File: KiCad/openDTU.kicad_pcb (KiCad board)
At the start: 2 copper layers, 50 x 50 mm, 12 parts, among them U1 ESP32NodeMCU, U2 NRF24L01+PA+LNA_Breakout

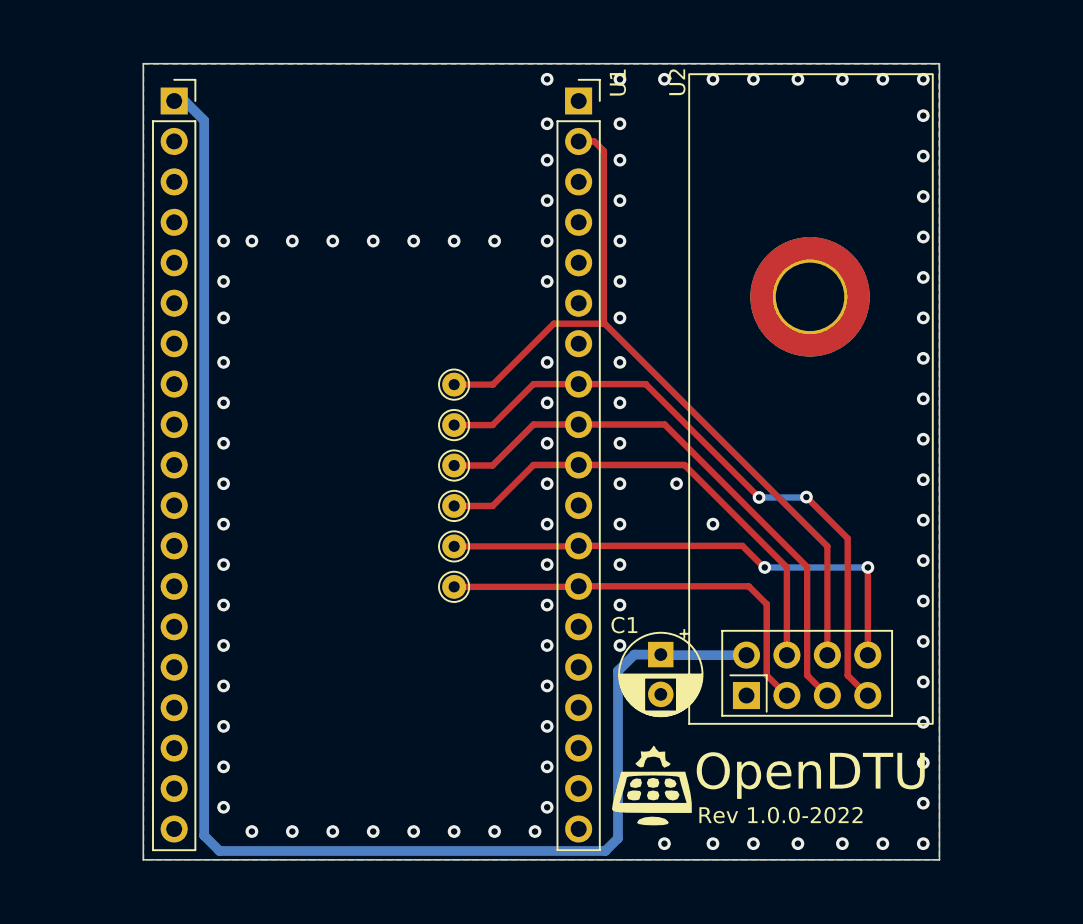
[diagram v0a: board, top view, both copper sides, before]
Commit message: Added mounting holes and some other improvments
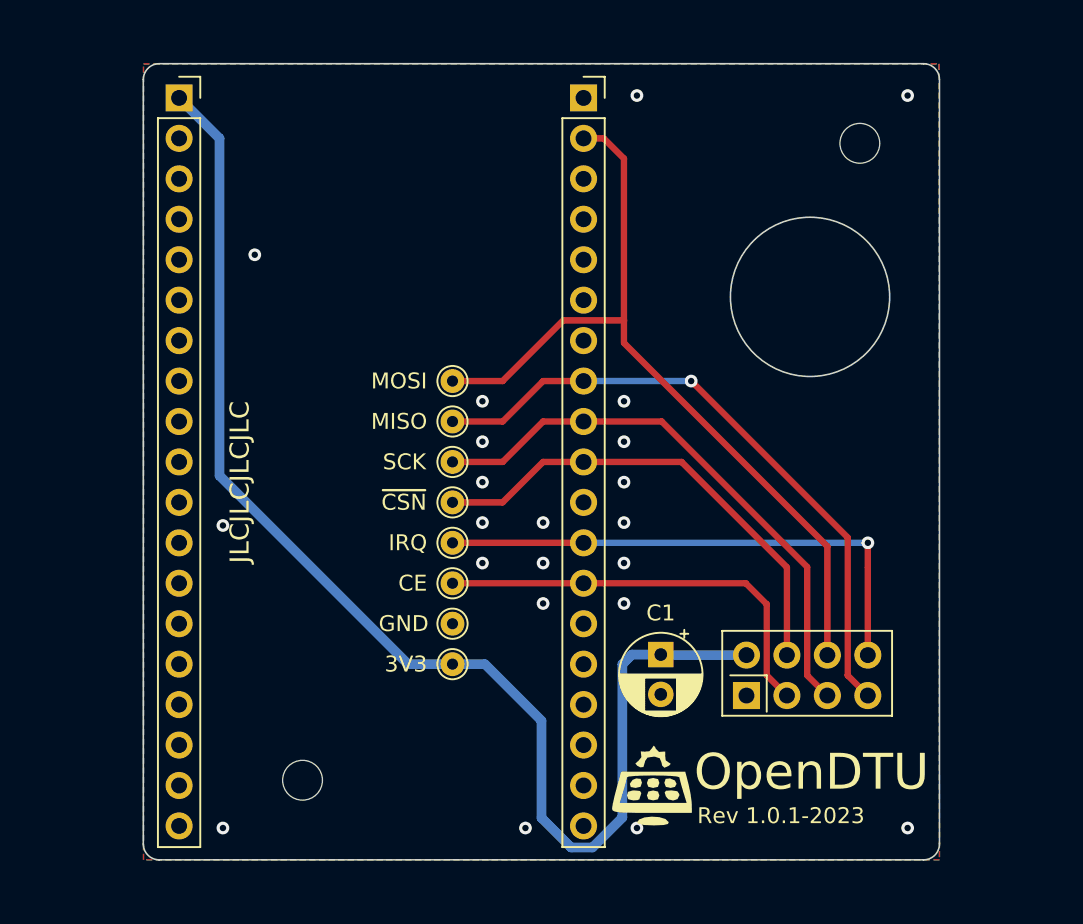
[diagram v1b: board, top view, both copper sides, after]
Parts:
- removed the REF** at (162.1, 85.0)
- added REF**: MountingHole_2.5mm, MountingHole:MountingHole_2.5mm, F.Cu at (165.2, 75.4)
- added REF**: MountingHole_2.5mm, MountingHole:MountingHole_2.5mm, F.Cu at (130.2, 115.4)
- added TP7: TestPoint, TestPoint:TestPoint_THTPad_D1.5mm_Drill0.7mm, F.Cu at (139.6, 108.1)
- added TP8: TestPoint, TestPoint:TestPoint_THTPad_D1.5mm_Drill0.7mm, F.Cu at (139.6, 105.6)
- moved REF** 19.1 mm to (159.3, 95.4)
- moved U1 0.36 mm to (122.4, 72.5)
- moved TP1 0.25 mm to (139.6, 90.3)
- moved TP4 0.25 mm to (139.6, 97.9)
- moved TP6 0.25 mm to (139.6, 103.0)
- moved TP2 0.25 mm to (139.6, 92.9)
- moved TP3 0.25 mm to (139.6, 95.4)
- moved TP5 0.25 mm to (139.6, 100.5)
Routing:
- net +3.3V: track 93.0 -> 81.8 mm
- net /MOSI: track 50.4 -> 51.9 mm
- net /IRQ: track 32.1 -> 33.2 mm, vias 2 -> 1
- net /MISO: track 40.2 -> 40.6 mm, vias 2 -> 1
- net GND: vias 97 -> 22
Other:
- outline, holes or cut-outs redrawn
- board text added: "JLCJLCJLCJLC"
- board text added: "Rev 1.0.1-2023"
- board text added: "github.com/dokuhn/openDTU-BreakoutBoard"
- board text removed: "Rev 1.0.0-2022"
- board text removed: "https://github.com/dokuhn/openDTU-BreakoutBoard"

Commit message: Added mounting holes
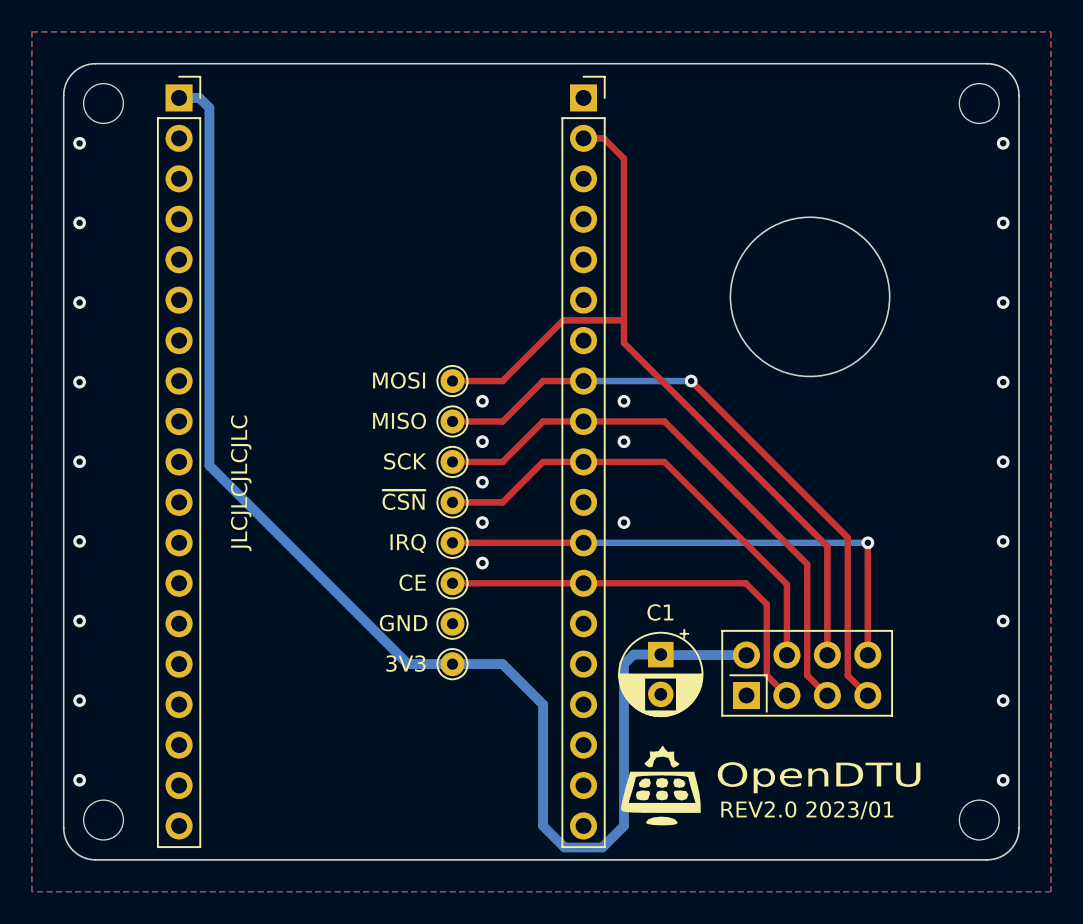
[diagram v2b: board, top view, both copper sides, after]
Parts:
- added G***: LOGO, OpenDTU_logo:OpenDTU, B.Cu at (168.2, 115.8)
- added REF**: MountingHole_2.5mm, MountingHole:MountingHole_2.5mm, F.Cu at (117.7, 72.9)
- added REF**: MountingHole_2.5mm, MountingHole:MountingHole_2.5mm, F.Cu at (172.7, 117.9)
- moved REF** 21.2 mm to (162.2, 74.4)
- moved REF** 12.7 mm to (117.7, 117.9)
- moved REF** 7.91 mm to (172.7, 72.9)
- moved G*** 0.56 mm to (152.7, 115.7)
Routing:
- net +3.3V: track 81.8 -> 83.7 mm
- net /~{CSN}: track 30.3 -> 29.7 mm
- net GND: vias 22 -> 26
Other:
- board size 50 x 50 mm -> 60 x 50 mm
- board text added: "REV2.0 2023/01"
- board text added: "github.com/foorschtbar/openDTU-BreakoutBoard"
- board text removed: "Rev 1.0.1-2023"
- board text removed: "github.com/dokuhn/openDTU-BreakoutBoard"
